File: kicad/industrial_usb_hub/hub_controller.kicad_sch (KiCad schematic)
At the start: 1 part, among them U1 USB5744-I_2G

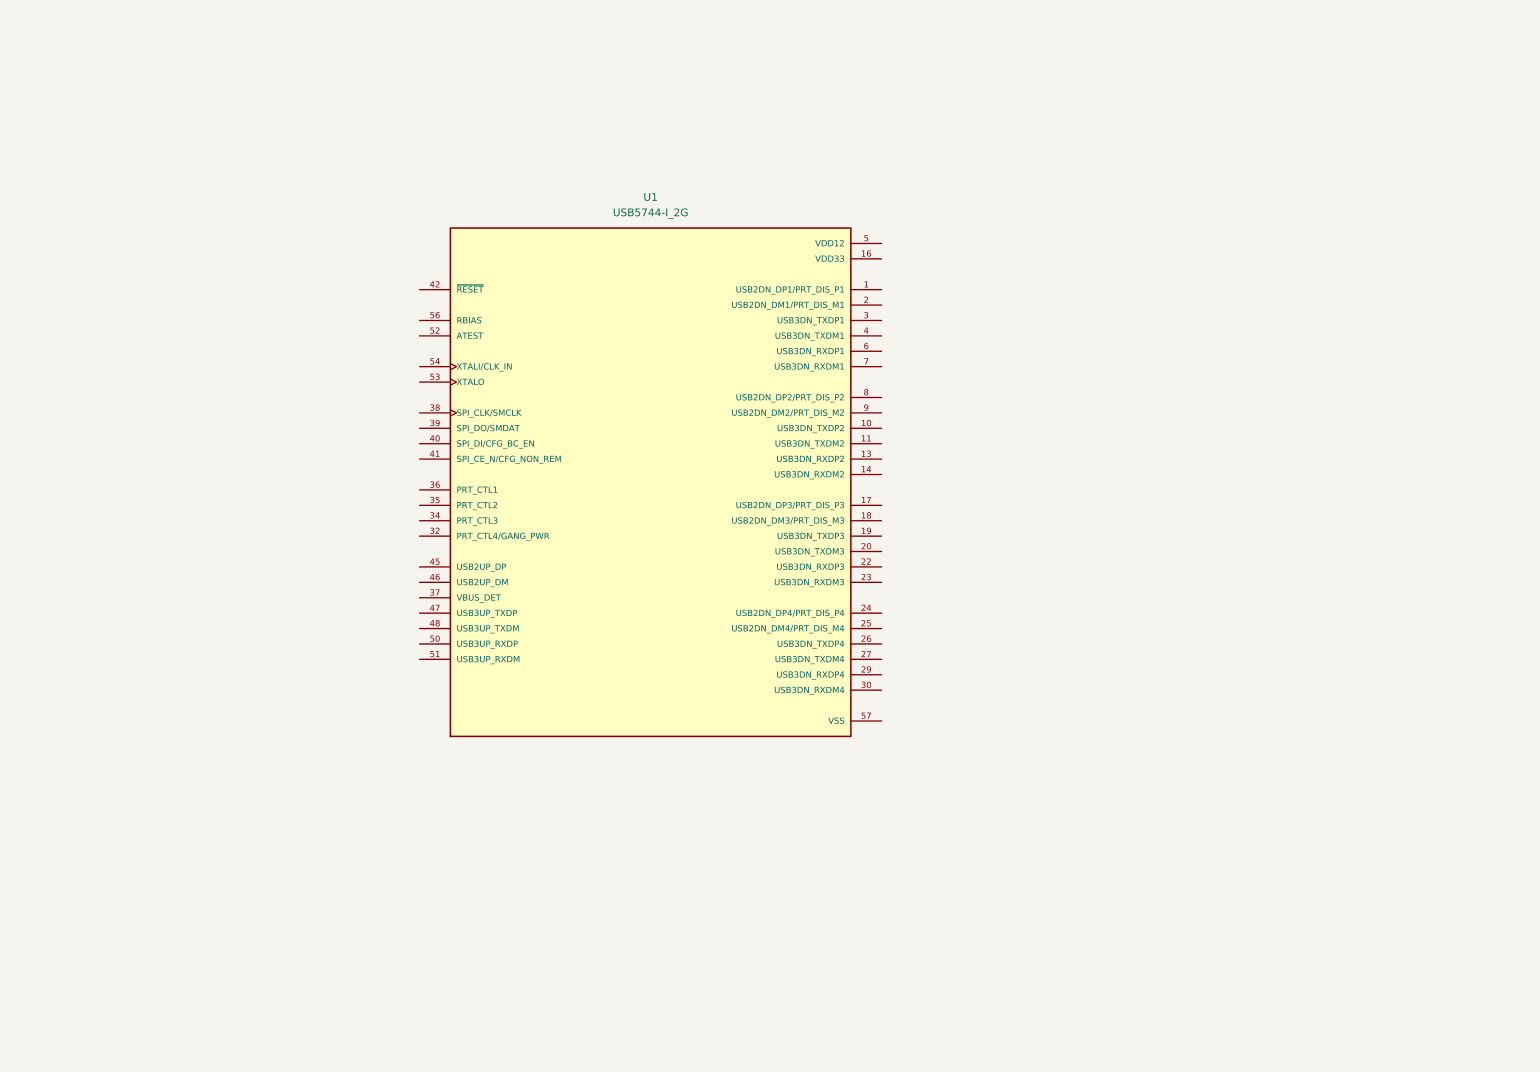
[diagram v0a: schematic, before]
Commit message: completed upstream circuit, moving on to power and downstream
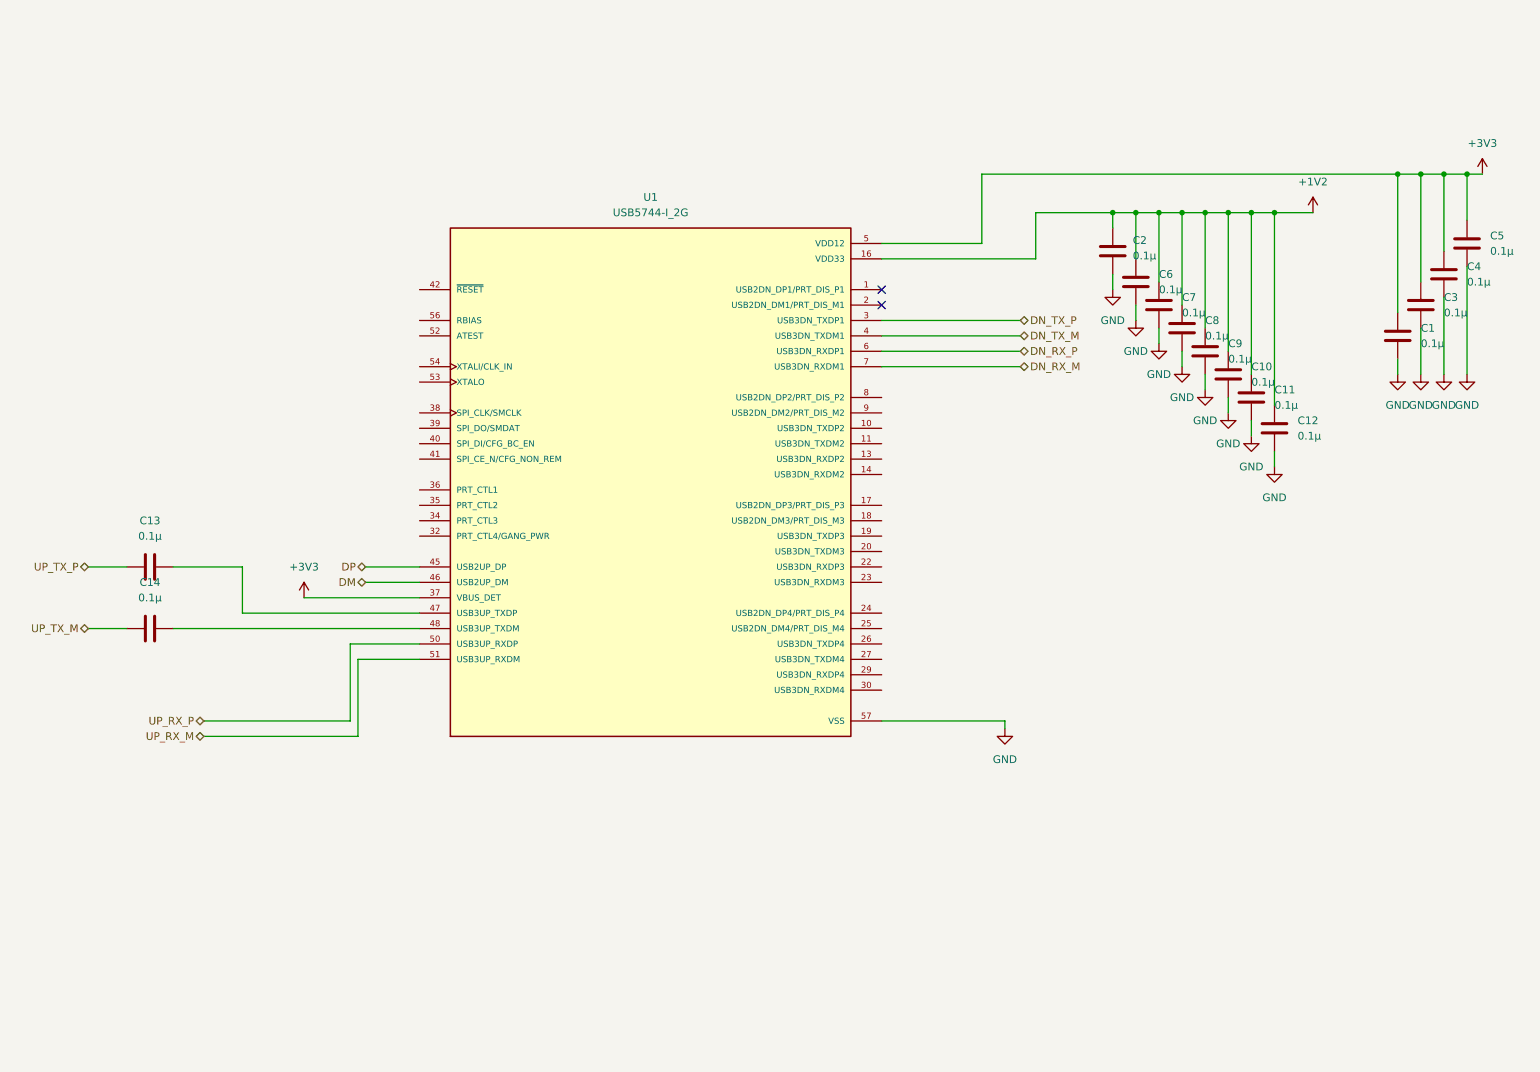
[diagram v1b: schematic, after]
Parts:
- added C1, C10, C11, C12, C13, C14, C2, C3, C4, C5, C6, C7, C8, C9: 0.1µ, Capacitor_SMD:C_0201_0603Metric, symbol Device:C
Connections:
- net VDD12 is gone; now on net +3V3: U1.12 (VDD12), U1.15 (VDD12), U1.21 (VDD12), U1.28 (VDD12), U1.33 (VDD12), U1.43 (VDD12), U1.49 (VDD12), U1.5 (VDD12)
- net DN_TX_P: now reaches U1.3 (USB3DN_TXDP1)
- net +3V3: now reaches U1.37 (VBUS_DET)
- net +3V3: now also C1.1, C3.1, C4.1, C5.1
- net DN_TX_M: now reaches U1.4 (USB3DN_TXDM1)
- net DP: now reaches U1.45 (USB2UP_DP)
- net DM: now reaches U1.46 (USB2UP_DM)
- net at U1.47 (USB3UP_TXDP): now also C13.2
- net at U1.48 (USB3UP_TXDM): now also C14.2
- net UP_RX_P: now reaches U1.50 (USB3UP_RXDP)
- net UP_RX_M: now reaches U1.51 (USB3UP_RXDM)
- net GND: now reaches U1.57 (VSS)
- net GND: now also C1.2, C10.2, C11.2, C12.2, C2.2, C3.2, C4.2, C5.2, C6.2, C7.2, C8.2, C9.2
- net DN_RX_P: now reaches U1.6 (USB3DN_RXDP1)
- net DN_RX_M: now reaches U1.7 (USB3DN_RXDM1)
- net VDD33 renamed +1V2
- net +1V2: now also C10.1, C11.1, C12.1, C2.1, C6.1, C7.1, C8.1, C9.1
- new net UP_TX_M: C14.1
- new net UP_TX_P: C13.1
- no-connect marks 0 -> 2

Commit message: completed schematic
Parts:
- added C17, C18, C25, C26, C27, C28, C29, C30: 0.1µ, Capacitor_SMD:C_0201_0603Metric, symbol Device:C
- added C21, C37: 10µ, Capacitor_SMD:C_0201_0603Metric, symbol Device:C
- added C23, C24: 33p, Capacitor_SMD:C_0201_0603Metric, symbol Device:C
- added R10, R13, R14: 10k, symbol Device:R
- added R11: 10, symbol Device:R
- added R12: 200k, symbol Device:R
- added R3: 43k, symbol Device:R
- added R4: 49.9k, symbol Device:R
- added R6: 12k, symbol Device:R
- added Y1: Crystal_GND24, personal_library:403I35D25M00000, symbol Device:Crystal_GND24
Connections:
- net +1V2: now also U1.12 (VDD12), U1.15 (VDD12), U1.21 (VDD12), U1.28 (VDD12), U1.33 (VDD12), U1.43 (VDD12), U1.49 (VDD12), U1.5 (VDD12); no longer U1.16 (VDD33), U1.31 (VDD33), U1.44 (VDD33), U1.55 (VDD33)
- net +3V3: now also U1.16 (VDD33), U1.31 (VDD33), U1.44 (VDD33), U1.55 (VDD33), R10.2; no longer U1.12 (VDD12), U1.15 (VDD12), U1.21 (VDD12), U1.28 (VDD12), U1.33 (VDD12), U1.37 (VBUS_DET), U1.43 (VDD12), U1.49 (VDD12), U1.5 (VDD12)
- net GND: now also U1.52 (ATEST), C21.1, C23.2, C24.2, C37.1, R11.1, R12.1, R13.1, R14.1, R4.1, R6.1, Y1.2 (G), Y1.4 (G)
- net DN_D_P1: now reaches U1.1 (USB2DN_DP1/PRT_DIS_P1)
- net at U1.10 (USB3DN_TXDP2): now also C25.1
- net at U1.11 (USB3DN_TXDM2): now also C26.1
- net DN_RX_P2: now reaches U1.13 (USB3DN_RXDP2)
- net DN_RX_N2: now reaches U1.14 (USB3DN_RXDM2)
- net DN_D_P3: now reaches U1.17 (USB2DN_DP3/PRT_DIS_P3)
- net DN_D_N3: now reaches U1.18 (USB2DN_DM3/PRT_DIS_M3)
- net at U1.19 (USB3DN_TXDP3): now also C27.1
- net DN_D_N1: now reaches U1.2 (USB2DN_DM1/PRT_DIS_M1)
- net at U1.20 (USB3DN_TXDM3): now also C28.1
- net DN_RX_P3: now reaches U1.22 (USB3DN_RXDP3)
- net DN_RX_N3: now reaches U1.23 (USB3DN_RXDM3)
- net DN_D_P4: now reaches U1.24 (USB2DN_DP4/PRT_DIS_P4)
- net DN_D_N4: now reaches U1.25 (USB2DN_DM4/PRT_DIS_M4)
- net at U1.26 (USB3DN_TXDP4): now also C29.1
- net at U1.27 (USB3DN_TXDM4): now also C30.1
- net DN_RX_P4: now reaches U1.29 (USB3DN_RXDP4)
- net DN_RX_N4: now reaches U1.30 (USB3DN_RXDM4)
- net PRT_CTL4: now reaches U1.32 (PRT_CTL4/GANG_PWR)
- net PRT_CTL3: now reaches U1.34 (PRT_CTL3)
- net PRT_CTL2: now reaches U1.35 (PRT_CTL2)
- net PRT_CTL1: now reaches U1.36 (PRT_CTL1)
- net SPI_CLK: now reaches U1.38 (SPI_CLK/SMCLK)
- net SPI_CLK: now also R14.2
- net SPI_DO: now reaches U1.39 (SPI_DO/SMDAT)
- net SPI_DO: now also R13.2
- net SPI_DI: now reaches U1.40 (SPI_DI/CFG_BC_EN)
- net SPI_DI: now also R11.2
- net SPI_CE_N: now reaches U1.41 (SPI_CE_N/CFG_NON_REM)
- net SPI_CE_N: now also R12.2
- net at U1.42 (~{RESET}): now also C37.2, R10.1
- net at U1.53 (XTALO): now also C24.1, Y1.1
- net at U1.54 (XTALI/CLK_IN): now also C23.1, Y1.3
- net at U1.56 (RBIAS): now also R6.2
- net DN_D_P2: now reaches U1.8 (USB2DN_DP2/PRT_DIS_P2)
- net DN_D_N2: now reaches U1.9 (USB2DN_DM2/PRT_DIS_M2)
- net DM renamed UP_D_N
- net DN_RX_M renamed DN_RX_N1
- net DN_RX_P renamed DN_RX_P1
- net DN_TX_M: no longer names the net of U1.4 (USB3DN_TXDM1)
- net DN_TX_M: now also C18.1
- net DN_TX_P: no longer names the net of U1.3 (USB3DN_TXDP1)
- net DN_TX_P: now also C17.1
- net DP renamed UP_D_P
- net UP_RX_M renamed UP_RX_N
- net UP_TX_M renamed UP_TX_N
- new net: R3.2, R4.2, U1.37 (VBUS_DET)
- new net DN_TX_N1: C18.2
- new net DN_TX_N2: C26.2
- new net DN_TX_N3: C28.2
- new net DN_TX_N4: C30.2
- new net DN_TX_P1: C17.2
- new net DN_TX_P2: C25.2
- new net DN_TX_P3: C27.2
- new net DN_TX_P4: C29.2
- new net VBUS: C21.2, R3.1
- no-connect marks 2 -> 0
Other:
- title: (none) -> Hub Controller
- moved on the sheet: C1, C10, C11, C12, C2, C3, C4, C5, C6, C7, C8, C9

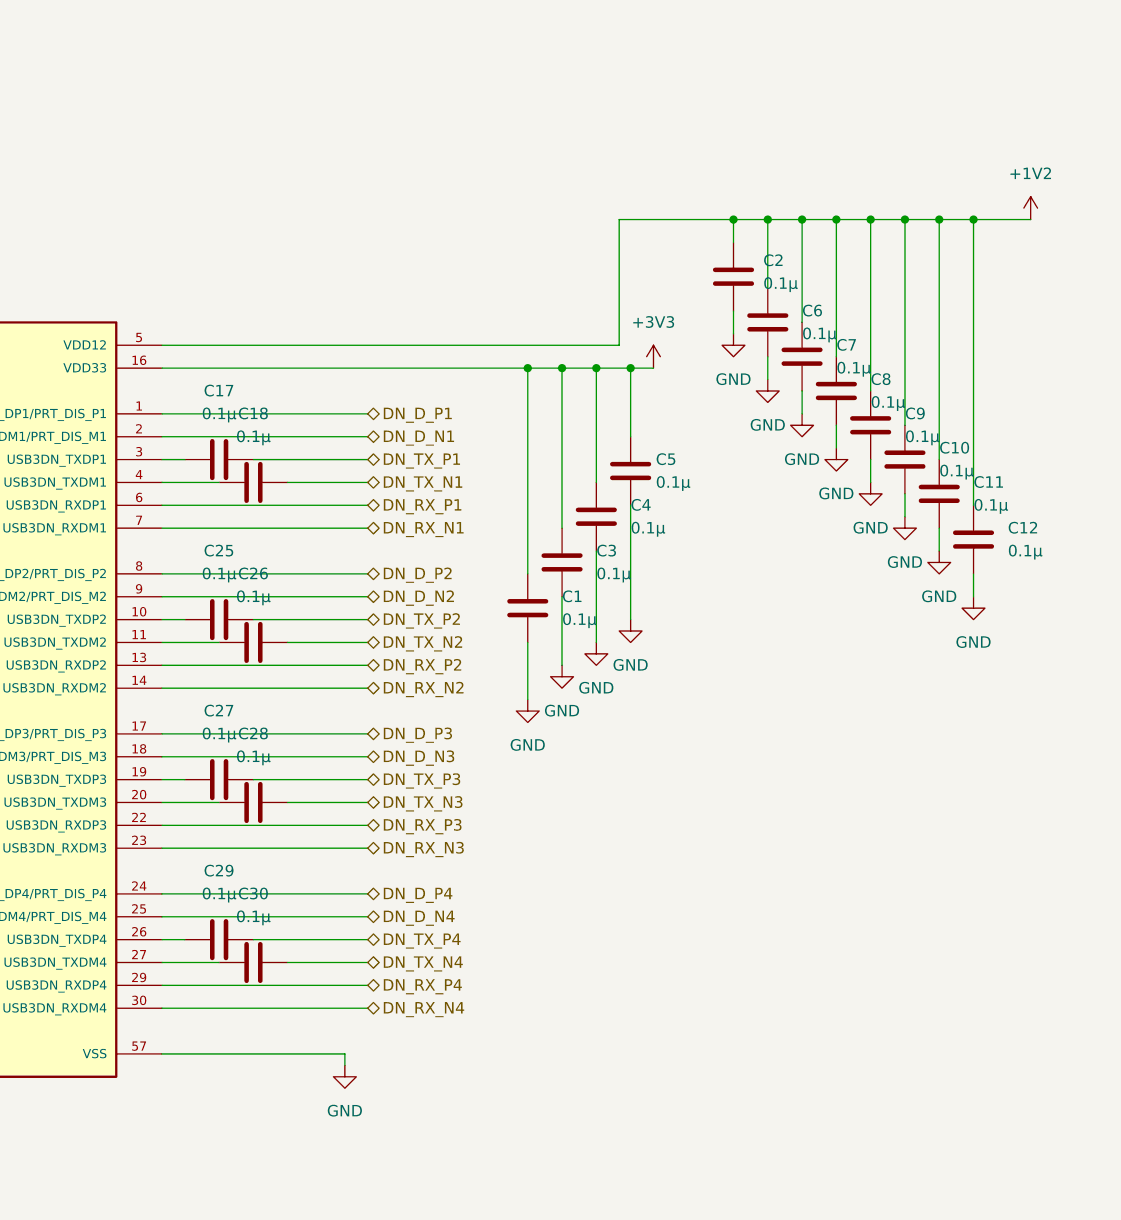
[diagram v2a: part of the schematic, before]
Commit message: assigned footprints
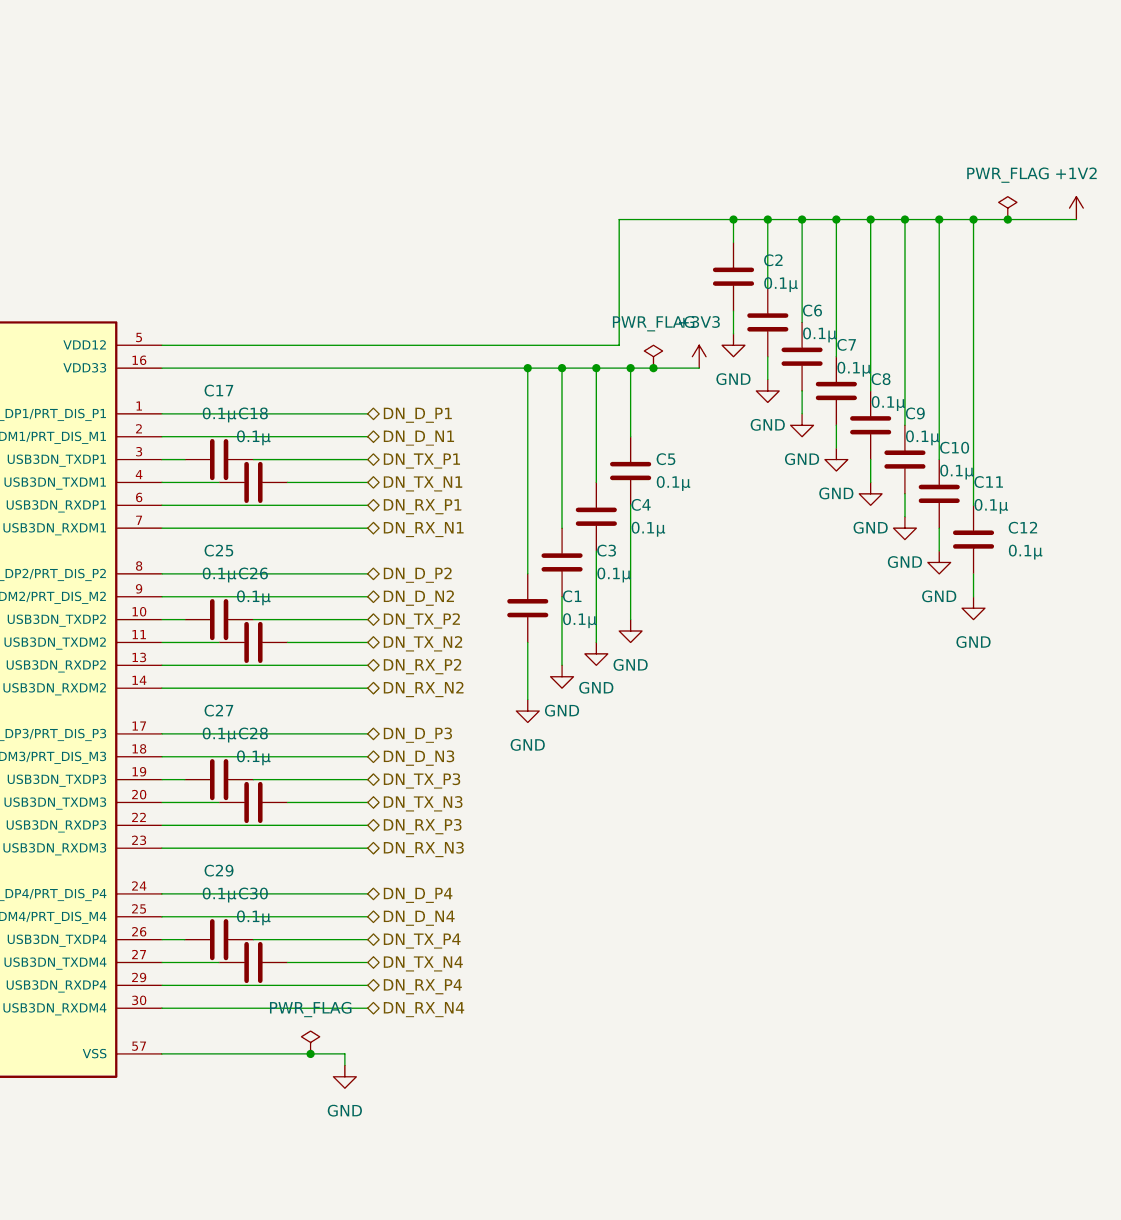
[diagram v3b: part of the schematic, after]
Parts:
- R10, R11, R12, R13, R14, R3, R4, R6: footprint (none) -> Resistor_SMD:R_0201_0603Metric
- U1: footprint USB5744-I_2G:QFN40P700X700X100-57N -> personal_library:USB5744-QFN40P700X700X100-57N

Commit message: okay okay it seems easier to do differential routing, feels menacing tho
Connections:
- net DN_TX_N4: now also C30.1, U1.27 (USB3DN_TXDM4)
- net DN_TX_P4: now also C29.1, U1.26 (USB3DN_TXDP4)
- net USB3UP_TXD_P: now reaches C13.2, U1.47 (USB3UP_TXDP)
- net USB3UP_TXD_N: now reaches C14.2, U1.48 (USB3UP_TXDM)
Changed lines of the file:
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@@
+		)
+	)
+	(label "USB3UP_TXD_N"
+		(at 83.82 118.11 0)
+		(effects
+			(font
+				(size 1.27 1.27)
+			)
+			(justify left bottom)
+		)
+	)
+	(label "DN_TX_P4"
+		(at 180.34 120.65 0)
+		(effects
+			(font
+				(size 1.27 1.27)
+			)
+			(justify left bottom)
 		)
 	)
@@
 		)
 	)
+	(label "DN_TX_N4"
+		(at 180.34 123.19 0)
+		(effects
+			(font
+				(size 1.27 1.27)
+			)
+			(justify left bottom)
+		)
+	)
+	(label "USB3UP_TXD_P"
+		(at 83.82 115.57 0)
+		(effects
+			(font
+				(size 1.27 1.27)
+			)
+			(justify left bottom)
+		)
+	)

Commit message: done routing, now fixing DRC errors (it's hatin)
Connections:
- net DN_TX_N4: no longer C30.1, U1.27 (USB3DN_TXDM4)
- net DN_TX_P4: no longer C29.1, U1.26 (USB3DN_TXDP4)
- net USB3_DN_TX_P1: now reaches C17.1, U1.3 (USB3DN_TXDP1)
- net USB3_DN_TX_N3: now reaches C28.1, U1.20 (USB3DN_TXDM3)
- net USB3_DN_TX_P2: now reaches C25.1, U1.10 (USB3DN_TXDP2)
- net USB3_DN_TX_N2: now reaches C26.1, U1.11 (USB3DN_TXDM2)
- net USB3_DN_TX_P3: now reaches C27.1, U1.19 (USB3DN_TXDP3)
- net USB3_DN_TX_N1: now reaches C18.1, U1.4 (USB3DN_TXDM1)
- new net USB3_DN_TX_N4: C30.1, U1.27 (USB3DN_TXDM4)
- new net USB3_DN_TX_P4: C29.1, U1.26 (USB3DN_TXDP4)
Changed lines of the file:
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@@
 		)
 	)
-	(label "DN_TX_P4"
+	(label "USB3_DN_TX_P4"
 		(at 180.34 120.65 0)
+		(effects
+			(font
+				(size 1.27 1.27)
+			)
+			(justify left bottom)
+		)
+	)
+	(label "USB3_DN_TX_N1"
+		(at 180.34 69.85 0)
 		(effects
 			(font
@@
 		)
 	)
+	(label "USB3_DN_TX_P1"
+		(at 180.34 67.31 0)
+		(effects
+			(font
+				(size 1.27 1.27)
+			)
+			(justify left bottom)
+		)
+	)
+	(label "USB3_DN_TX_P3"
+		(at 180.34 102.87 0)
+		(effects
+			(font
+				(size 1.27 1.27)
+			)
+			(justify left bottom)
+		)
+	)
 	(label "SPI_CE_N"
 		(at 100.33 90.17 180)
@@
 		)
 	)
-	(label "DN_TX_N4"
+	(label "USB3_DN_TX_N2"
+		(at 181.61 87.63 0)
+		(effects
+			(font
+				(size 1.27 1.27)
+			)
+			(justify left bottom)
+		)
+	)
+	(label "USB3_DN_TX_N4"
 		(at 180.34 123.19 0)
 		(effects
@@
 		)
 	)
+	(label "USB3_DN_TX_N3"
+		(at 180.34 105.41 0)
+		(effects
+			(font
+				(size 1.27 1.27)
+			)
+			(justify left bottom)
+		)
+	)
+	(label "USB3_DN_TX_P2"
+		(at 181.61 85.09 0)
+		(effects
+			(font
+				(size 1.27 1.27)
+			)
+			(justify left bottom)
+		)
+	)
